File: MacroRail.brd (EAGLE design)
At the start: 42.9 x 81.5 mm, 21 parts, among them CN2 1X4-3.5MM, CN3 SJ1-2503A, U1 ESP32DEVKITC, U2 TMC2209-V1.2+INDEX

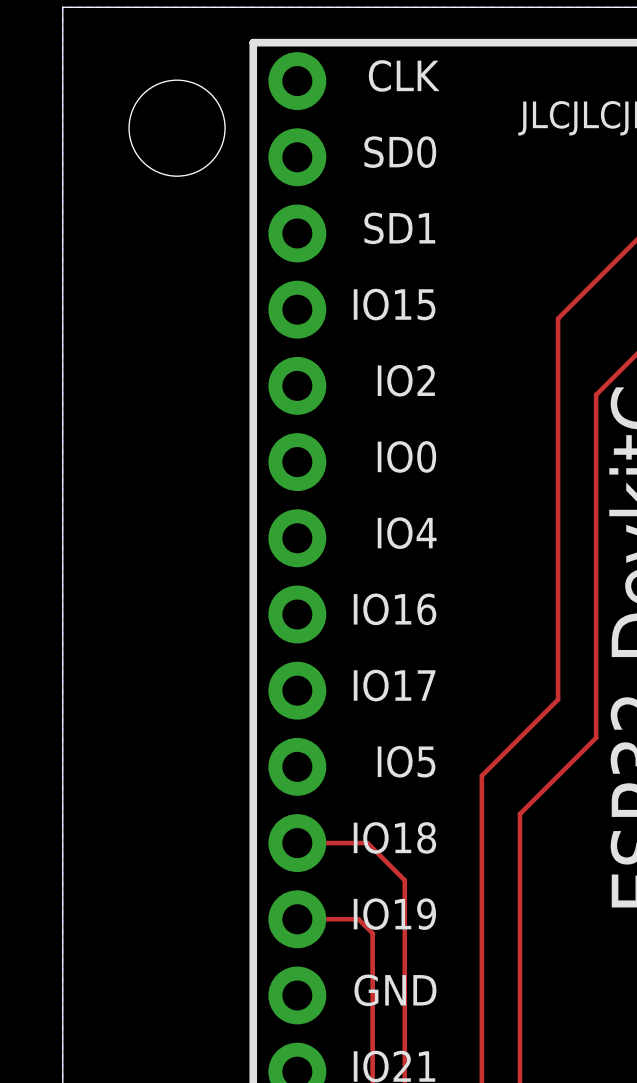
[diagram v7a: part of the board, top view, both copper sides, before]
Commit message: Add possibility for driving high power LEDs
Since good illumination is important for macro photography, an option to drive high power LEDs via the Motorized Macro Rail PCB has been added.
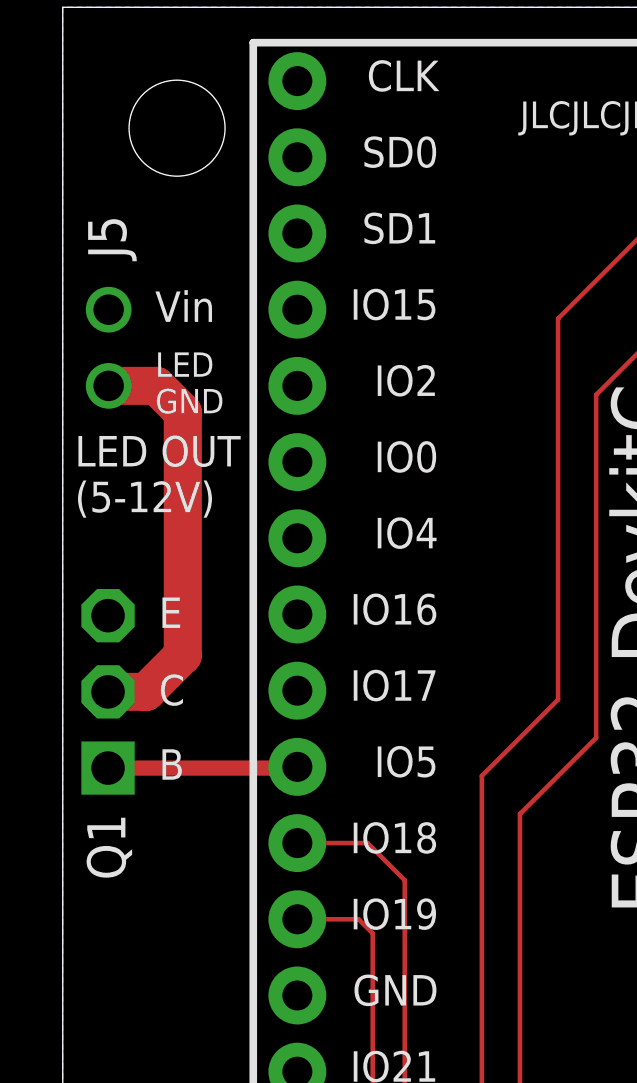
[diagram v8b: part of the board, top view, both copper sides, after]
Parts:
- added J5: (no value), pinhead-custom:1X02CLEAN
- added Q1: TIP120, 00-Random-Components-Simen:TO220AH
- moved U$3 7.62 mm to (3.81, 34.3)
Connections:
- new net LED_GND: J5.2, Q1.C
- new net LED_PWM: Q1.B, U1.29
- net GND: now also Q1.E
- net V_MOTOR: now also J5.1
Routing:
- net LED_GND: track 0.00 -> 13.9 mm
- net LED_PWM: track 0.00 -> 6.33 mm
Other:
- board text added: "B"
- board text added: "C"
- board text added: "E"
- board text added: "LED GND"
- board text added: "LED OUT (5-12V)"
- board text added: "Vin"
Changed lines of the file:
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@@
 </layers>
 <board>
-<fusionsync huburn="a.cGVyc29uYWw6dWUyYjkwZjE2" projecturn="a.cGVyc29uYWw6dWUyYjkwZjE2IzIwMTgwOTA0MTQ2OTc5MDgx" f3durn="urn:adsk.wipprod:dm.lineage:p6BxFAy9R-OurxXYLrTLuw" pcbguid="dc448735-d099-4600-9fa7-d1462ebbee2b" lastpulledtime="" lastsyncedchangeguid="1bc08179-7a2f-3cd6-9f80-1574863fa7a8"/>
+<fusionsync huburn="a.cGVyc29uYWw6dWUyYjkwZjE2" projecturn="a.cGVyc29uYWw6dWUyYjkwZjE2IzIwMTgwOTA0MTQ2OTc5MDgx" f3durn="urn:adsk.wipprod:dm.lineage:p6BxFAy9R-OurxXYLrTLuw" pcbguid="dc448735-d099-4600-9fa7-d1462ebbee2b" lastpulledtime="" lastsyncedchangeguid="2ab9a09d-8338-4cc2-c5d5-c756458d8fb4"/>
 <plain>
 <wire x1="0" y1="0" x2="42.85" y2="0" width="0" layer="20"/>
@@
 <text x="39.37" y="57.46" size="1.27" layer="25" align="center-right">LIMIT1</text>
 <text x="39.37" y="68.89" size="1.27" layer="25" align="center-right">LIMIT2</text>
-<text x="5.588" y="45.974" size="1.778" layer="26" rot="SMR270" align="bottom-right">Simen E. Sørensen</text>
-<text x="3.048" y="45.974" size="1.778" layer="26" rot="SMR270" align="bottom-right">Mar 2022</text>
+<text x="5.588" y="38.354" size="1.778" layer="26" rot="SMR270" align="bottom-right">Simen E. Sørensen</text>
+<text x="3.048" y="38.354" size="1.778" layer="26" rot="SMR270" align="bottom-right">Mar 2022</text>
 <dimension x1="42.85" y1="81.5" x2="0" y2="81.5" x3="21.425" y3="86.36" textsize="1.778" layer="48"/>
 <dimension x1="0" y1="81.5" x2="0" y2="0" x3="-3.81" y3="40.75" textsize="1.778" layer="48"/>
@@
 <wire x1="26.9" y1="22" x2="27.1" y2="22" width="0.1524" layer="26"/>
 <wire x1="27.5" y1="21.9" x2="25.4" y2="21.9" width="0.1524" layer="26"/>
+<text x="3.98" y="72.07" size="1.016" layer="22" rot="MR0" align="top-center">Vin</text>
+<text x="3.92" y="69.88" size="0.8128" layer="22" rot="MR0" align="top-center">LED
+GND</text>
+<text x="0.4" y="64.67" size="1.016" layer="21">LED OUT
+(5-12V)</text>
+<text x="3.2" y="56.26" size="1.016" layer="21" align="center-left">B</text>
+<text x="3.2" y="58.74" size="1.016" layer="21" align="center-left">C</text>
+<text x="3.2" y="61.32" size="1.016" layer="21" align="center-left">E</text>
+<text x="3.08" y="71.52" size="1.016" layer="21" align="center-left">Vin</text>
+<text x="3.08" y="68.98" size="0.8128" layer="21" align="center-left">LED
+GND</text>
 </plain>
 <attributes>
@@
 </element>
 <element name="U$2" library="Silkscreen-art" package="APPLIED-PROCRASTINATION-FULL" value="" x="21.59" y="73.66" smashed="yes" rot="MR270"/>
-<element name="U$3" library="SparkFun-Aesthetics" library_urn="urn:adsk.eagle:library:507" package="OSHW-LOGO-M" package3d_urn="urn:adsk.eagle:package:37126/1" value="" x="3.81" y="41.91" smashed="yes" rot="MR270"/>
+<element name="U$3" library="SparkFun-Aesthetics" library_urn="urn:adsk.eagle:library:507" package="OSHW-LOGO-M" package3d_urn="urn:adsk.eagle:package:37126/1" value="" x="3.81" y="34.29" smashed="yes" rot="MR270"/>
 <element name="OK1" library="optocoupler" library_urn="urn:adsk.eagle:library:320" package="DIL04" package3d_urn="urn:adsk.eagle:package:21938/1" override_package3d_urn="urn:adsk.eagle:package:34319665/2" override_package_urn="urn:adsk.eagle:footprint:21858/1" value="PC817" x="39.37" y="29.21" smashed="yes" rot="R180">
 <attribute name="MF" value="" x="39.37" y="29.21" size="0.889" layer="27" rot="R180" display="off"/>
@@
 <attribute name="SPICEPREFIX" value="R" x="17.78" y="29.21" size="1.778" layer="27" rot="R180" display="off"/>
 <attribute name="VALUE" x="20.066" y="29.7688" size="1.27" layer="27" ratio="10" rot="R180"/>
+</element>
+<element name="Q1" library="00-Random-Components-Simen" library_urn="urn:adsk.eagle:library:24319138" package="TO220AH" package3d_urn="urn:adsk.eagle:package:34683657/2" override_package3d_urn="urn:adsk.eagle:package:34684429/2" override_package_urn="urn:adsk.eagle:footprint:34683656/2" value="TIP120" x="1.51" y="56.14" smashed="yes" rot="R90">
+<attribute name="NAME" x="1.453" y="54.63" size="1.27" layer="25" ratio="10" rot="R90" align="center-right"/>
+<attribute name="POPULARITY" value="2" x="1.51" y="56.14" size="1.778" layer="27" rot="R90" display="off"/>
+<attribute name="VALUE" x="5.32" y="54.743" size="1.778" layer="27" ratio="10" rot="R90"/>
+</element>
+<element name="J5" library="pinhead-custom" library_urn="urn:adsk.eagle:library:7941324" package="1X02CLEAN" override_package3d_urn="urn:adsk.eagle:package:34684443/2" override_package_urn="urn:adsk.eagle:footprint:34684444/1" value="" x="1.53" y="70.15" smashed="yes" rot="R270">
+<attribute name="NAME" x="1.4812" y="73.1138" size="1.27" layer="25" ratio="10" rot="R90" align="center-left"/>
+<attribute name="VALUE" x="-1.645" y="72.69" size="1.27" layer="27" rot="R270"/>
 </element>
 </elements>
@@
 </polygon>
 <contactref element="C2" pad="2"/>
+<contactref element="J5" pad="1"/>
 </signal>
 <signal name="GND" class="1">
@@
 <contactref element="OK1" pad="2"/>
 <contactref element="C2" pad="1"/>
+<contactref element="Q1" pad="E"/>
 </signal>
 <signal name="A2" class="1">
@@
 <wire x1="26.67" y1="31.75" x2="26.67" y2="52.07" width="0.1524" layer="1"/>
 </signal>
+<signal name="LED_PWM">
+<contactref element="Q1" pad="B"/>
+<contactref element="U1" pad="29"/>
+<wire x1="1.51" y1="56.14" x2="7.78" y2="56.14" width="0.508" layer="1"/>
+<wire x1="7.78" y1="56.14" x2="7.82" y2="56.18" width="0.508" layer="1"/>
+</signal>
+<signal name="LED_GND">
+<contactref element="Q1" pad="C"/>
+<contactref element="J5" pad="2"/>
+<wire x1="1.53" y1="68.88" x2="3.12" y2="68.88" width="1.27" layer="1"/>
+<wire x1="3.12" y1="68.88" x2="4" y2="68" width="1.27" layer="1"/>
+<wire x1="4" y1="68" x2="4" y2="59.9" width="1.27" layer="1"/>
+<wire x1="2.78" y1="58.68" x2="1.51" y2="58.68" width="1.27" layer="1"/>
+<wire x1="4" y1="59.9" x2="2.78" y2="58.68" width="1.27" layer="1"/>
+</signal>
 </signals>
